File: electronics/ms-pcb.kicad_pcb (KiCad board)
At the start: 2 copper layers, 110 x 110 mm, 39 parts, among them J1 Left motor, J2 Right motor, J3 XT60-M, U1 ESP32-S3-DEVKITC-1U-N8R2, U2 GY-521

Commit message: docs: fix v1.1.0 pin mapping
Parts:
- R4: value 30k -> 10k
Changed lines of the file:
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@@
 			)
 		)
-		(property "Value" "30k"
+		(property "Value" "10k"
 			(at 0 1.82 180)
 			(layer "F.Fab")

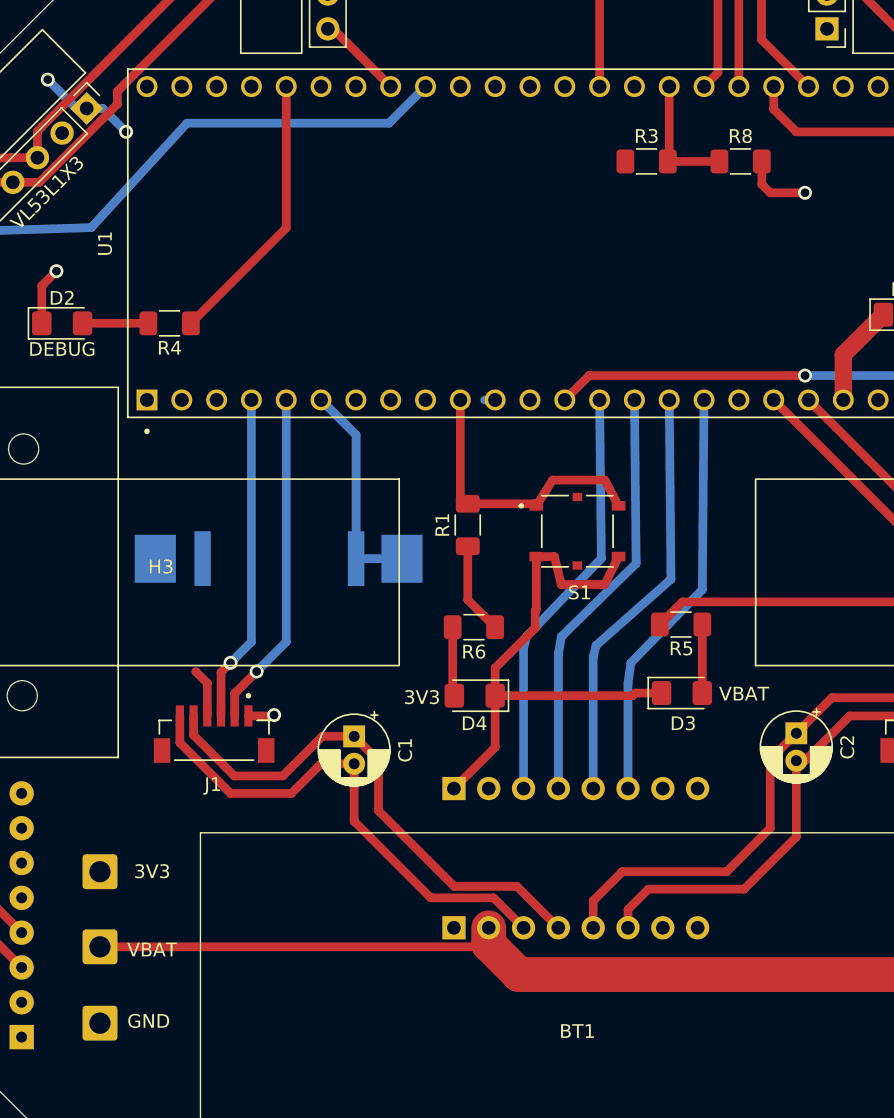
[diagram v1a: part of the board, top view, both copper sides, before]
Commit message: elec: fix vcc voltage measurement pin
Closes: #66
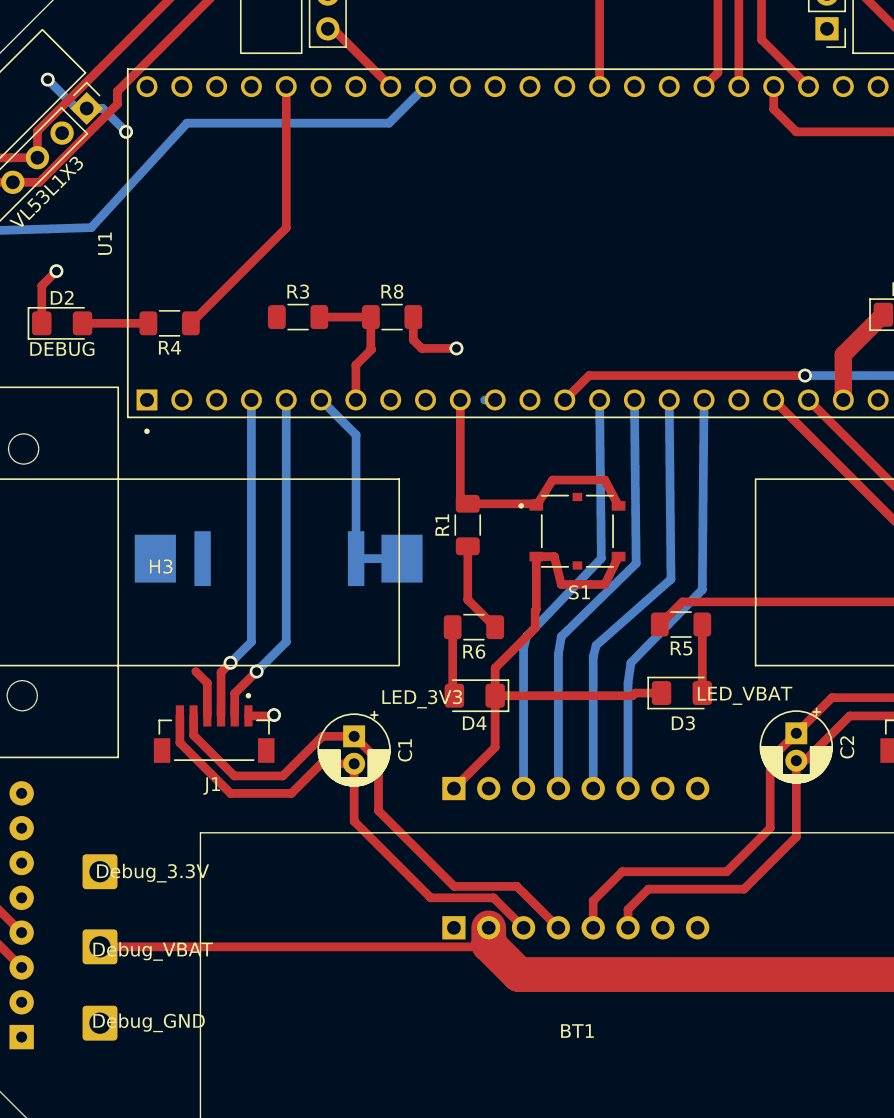
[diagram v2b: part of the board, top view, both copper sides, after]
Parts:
- D3: value VBAT -> LED_VBAT
- D4: value 3V3 -> LED_3V3
- H7: value 3V3 -> Debug_3.3V
- H8: value VBAT -> Debug_VBAT
- H9: value GND -> Debug_GND
- R5: value 30k -> 40k
- moved R3 27.8 mm to (104.6, 76.4)
- moved R8 27.8 mm to (111.5, 76.4)
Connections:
- U1 pad J1_7: unconnected-(U1-GPIO7-PadJ1_7) -> Mes_VCC
- U1 pad J3_16: Mes_VCC -> unconnected-(U1-GPIO48-PadJ3_16)
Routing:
- net Mes_VCC: track 9.26 -> 10.4 mm
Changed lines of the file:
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@@
 	(net 36 "button")
 	(net 37 "unconnected-(U1-GPIO8-PadJ1_12)")
-	(net 38 "unconnected-(U1-GPIO7-PadJ1_7)")
+	(net 38 "unconnected-(U1-GPIO48-PadJ3_16)")
 	(net 39 "unconnected-(U1-U0TXD{slash}GPIO43-PadJ3_2)")
 	(net 40 "unconnected-(U1-GPIO15-PadJ1_8)")
@@
 			)
 		)
-		(property "Description" "yellow"
+		(property "Description" ""
 			(at 0 0 0)
 			(unlocked yes)
@@
 	(footprint "Resistor_SMD:R_1206_3216Metric_Pad1.30x1.75mm_HandSolder"
 		(layer "F.Cu")
-		(at 130.048 65.024)
+		(at 104.622 76.3775)
 		(descr "Resistor SMD 1206 (3216 Metric), square (rectangular) end terminal, IPC_7351 nominal with elongated pad for handsoldering. (Body size source: IPC-SM-782 page 72, https://www.pcb-3d.com/wordpress/wp-content/uploads/ipc-sm-782a_amendment_1_and_2.pdf), generated with kicad-footprint-generator")
 		(tags "resistor handsolder")
@@
 			)
 		)
-		(property "Value" "GND"
+		(property "Value" "Debug_GND"
 			(at 3.556 -0.127 0)
 			(layer "F.SilkS")
@@
 			)
 		)
-		(property "Value" "3V3"
+		(property "Value" "Debug_3.3V"
 			(at 3.81 0 0)
 			(layer "F.SilkS")
@@
 	(footprint "Resistor_SMD:R_1206_3216Metric_Pad1.30x1.75mm_HandSolder"
 		(layer "F.Cu")
-		(at 136.906 65.024)
+		(at 111.48 76.3775)
 		(descr "Resistor SMD 1206 (3216 Metric), square (rectangular) end terminal, IPC_7351 nominal with elongated pad for handsoldering. (Body size source: IPC-SM-782 page 72, https://www.pcb-3d.com/wordpress/wp-content/uploads/ipc-sm-782a_amendment_1_and_2.pdf), generated with kicad-footprint-generator")
 		(tags "resistor handsolder")
@@
 			)
 		)
-		(property "Value" "3V3"
+		(property "Value" "LED_3V3"
 			(at 3.8475 -0.14 180)
 			(layer "F.SilkS")
@@
 			)
 		)
-		(property "Description" "blue"
+		(property "Description" ""
 			(at 0 0 180)
 			(unlocked yes)
@@
 			)
 		)
-		(property "Value" "VBAT"
+		(property "Value" "LED_VBAT"
 			(at 4.5355 0.08 0)
 			(layer "F.SilkS")
@@
 			)
 		)
-		(property "Description" "green"
+		(property "Description" ""
 			(at 0 0 0)
 			(unlocked yes)
@@
 			)
 		)
-		(property "Value" "30k"
+		(property "Value" "40k"
 			(at 0 -1.778 0)
 			(layer "F.Fab")
@@
 			)
 		)
+		(sheetname "Root")
+		(sheetfile "ms-pcb.kicad_sch")
 		(attr through_hole)
 		(fp_line
@@
 			(layers "*.Cu" "*.Mask")
 			(remove_unused_layers no)
-			(net 38 "unconnected-(U1-GPIO7-PadJ1_7)")
+			(net 55 "Mes_VCC")
 			(pinfunction "GPIO7")
-			(pintype "bidirectional+no_connect")
+			(pintype "bidirectional")
 			(solder_mask_margin 0.102)
 		)
@@
 			(layers "*.Cu" "*.Mask")
 			(remove_unused_layers no)
-			(net 55 "Mes_VCC")
+			(net 38 "unconnected-(U1-GPIO48-PadJ3_16)")
 			(pinfunction "GPIO48")
-			(pintype "bidirectional")
+			(pintype "bidirectional+no_connect")
 			(solder_mask_margin 0.102)
 		)
@@
 			)
 		)
-		(property "Value" "VBAT"
+		(property "Value" "Debug_VBAT"
 			(at 3.81 0.235 0)
 			(layer "F.SilkS")
@@
 	)
 	(segment
-		(start 138.456 66.701)
-		(end 139.065 67.31)
+		(start 113.03 78.0545)
+		(end 113.639 78.6635)
 		(width 0.635)
 		(layer "F.Cu")
@@
 	)
 	(segment
-		(start 138.456 65.024)
-		(end 138.456 66.701)
+		(start 113.03 76.3775)
+		(end 113.03 78.0545)
 		(width 0.635)
 		(layer "F.Cu")
@@
 	)
 	(segment
-		(start 139.065 67.31)
-		(end 141.605 67.31)
+		(start 113.639 78.6635)
+		(end 116.179 78.6635)
 		(width 0.635)
 		(layer "F.Cu")
@@
 	)
 	(via
-		(at 141.605 67.31)
+		(at 116.179 78.6635)
 		(size 1.016)
 		(drill 0.635)
@@
 	)
 	(segment
-		(start 131.699 59.563)
-		(end 131.699 64.923)
+		(start 108.839 82.423)
+		(end 108.839 79.883)
+		(width 0.635)
+		(layer "F.Cu")
+		(net 55)
+	)
+	(segment
+		(start 109.982 78.74)
+		(end 109.93 78.688)
+		(width 0.635)
+		(layer "F.Cu")
+		(net 55)
+	)
+	(segment
+		(start 108.839 79.883)
+		(end 109.982 78.74)
+		(width 0.635)
+		(layer "F.Cu")
+		(net 55)
+	)
+	(segment
+		(start 109.93 78.688)
+		(end 109.93 76.3775)
 		(width 0.635)
 		(layer "F.Cu")
@@
 	)
 	(segment
-		(start 131.598 65.024)
-		(end 135.356 65.024)
+		(start 106.172 76.3775)
+		(end 109.93 76.3775)
 		(width 0.635)
 		(layer "F.Cu")
@@
 	)
 	(segment
-		(start 131.699 64.923)
-		(end 131.598 65.024)
+		(start 106.273 76.2765)
+		(end 106.172 76.3775)
 		(width 0.635)
 		(layer "F.Cu")
